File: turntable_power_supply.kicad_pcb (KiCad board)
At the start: 2 copper layers, 65 x 56 mm, 30 parts, among them IC15 171032401, IC235 171032401, IC5 171032401, X15 694106301002, X235 694106301002, X24 694106301002, X5 PRT-21570

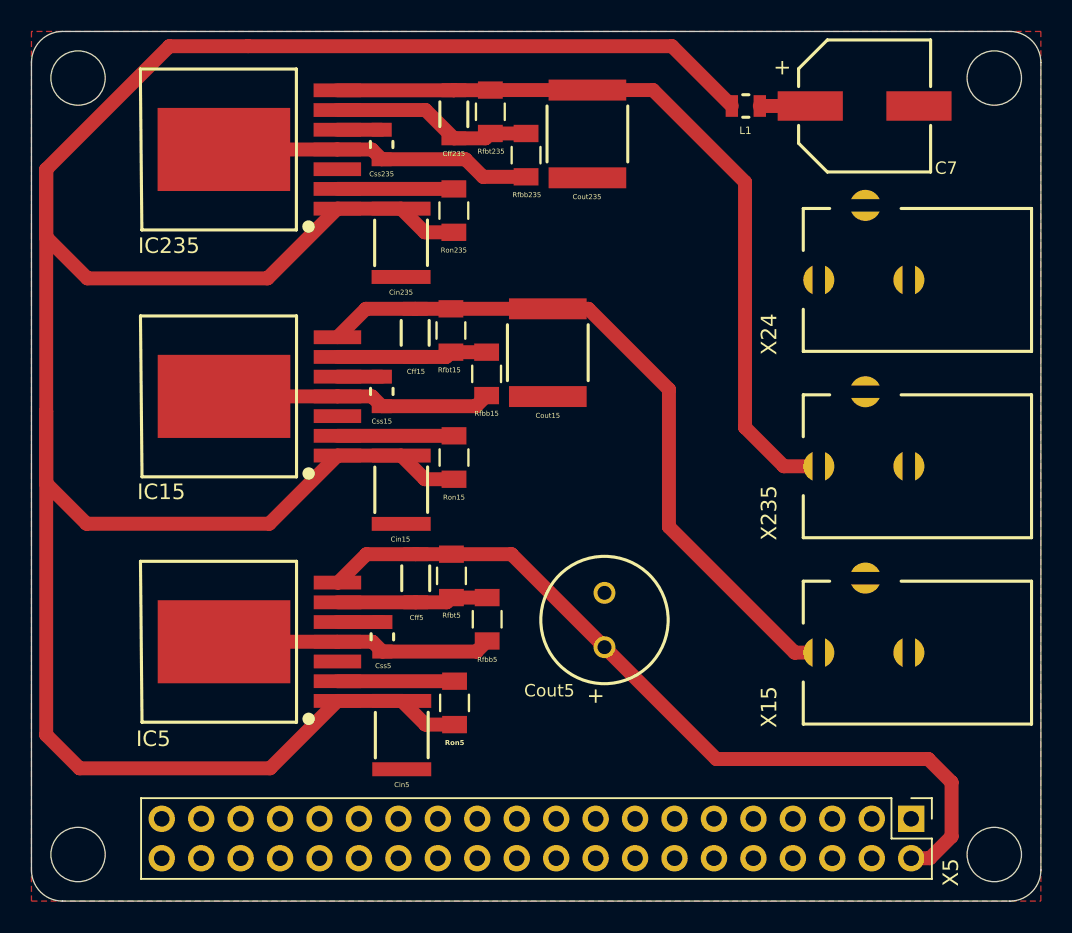
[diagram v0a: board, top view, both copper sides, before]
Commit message: Add missing capacitors
Signed-off-by: Marc 'risson' Schmitt <marc.schmitt@risson.space>
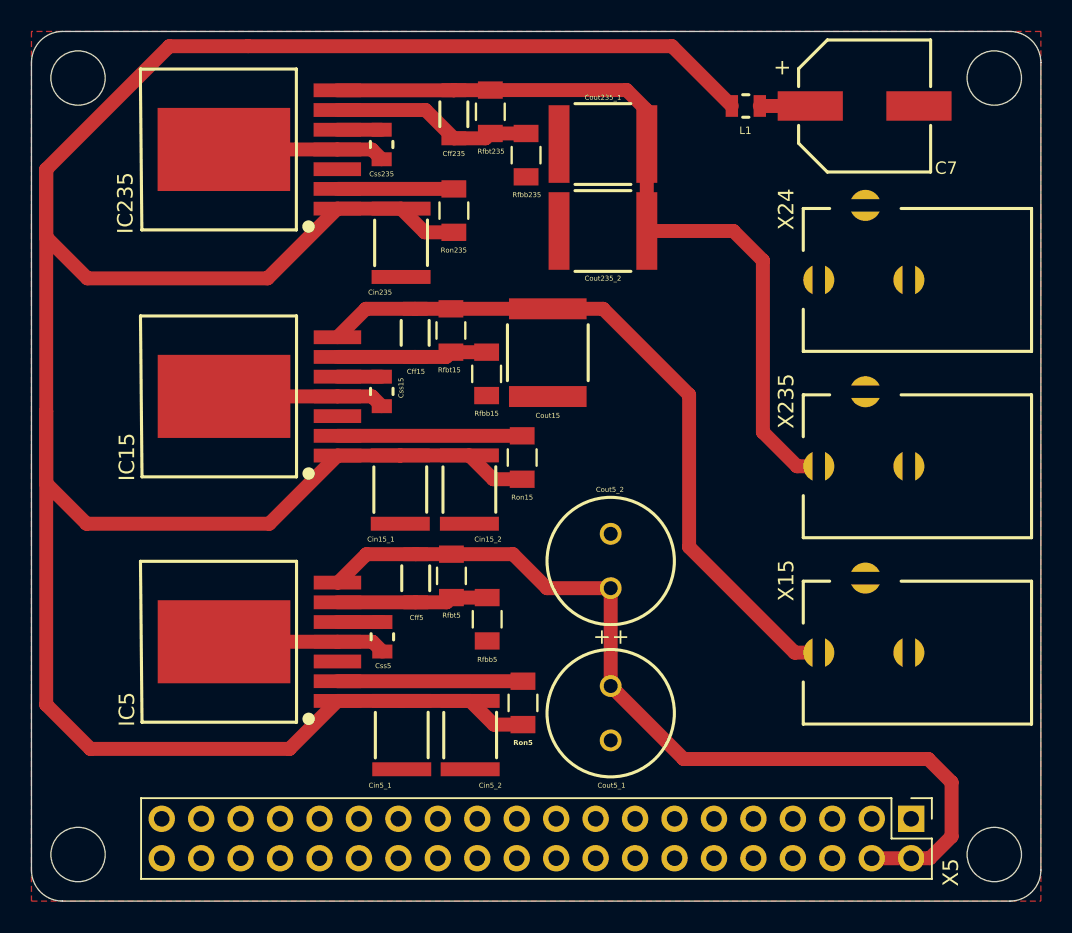
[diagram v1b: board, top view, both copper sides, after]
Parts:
- added Cin15_2: 2.2uF, 885012210032:885012210032, F.Cu at (148.2, 99.0)
- added Cin5_2: 2.2uF, 885012210032:885012210032, F.Cu at (148.2, 114.8)
- added Cout235_2: 10uF, 885012214006:885012214006, F.Cu at (156.8, 82.3)
- added Cout5_2: 68uF, 870235674004:870235674004, F.Cu at (157.3, 103.6)
- moved Cout5_1 6.01 mm to (157.3, 113.4), turned to 90 degrees
- moved Ron5 4.41 mm to (151.7, 112.7)
- moved Ron15 4.39 mm to (151.6, 96.9)
- moved Cout235_1 1.19 mm to (156.8, 76.8), turned to 180 degrees
- moved Cin15_1 0.06 mm to (143.8, 99.0)
- renumbered Cin15 to Cin15_1, Cin5 to Cin5_1, Cout235 to Cout235_1, Cout5 to Cout5_1
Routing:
- net GND: track 55.1 -> 31.3 mm
- net +24V: track 183.7 -> 190.3 mm
- net +5V: track 53.1 -> 59.3 mm
- net Net-(IC5-Pad2): track 7.54 -> 11.9 mm
- net Net-(IC15-Pad2): track 7.50 -> 11.9 mm
- net +23.5V: track 50.3 -> 52.1 mm
- net +15V: track 47.1 -> 47.6 mm
